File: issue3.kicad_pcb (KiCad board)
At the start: 2 copper layers, 213.1 x 129 mm, 206 parts, among them IC1 ULA, IC10 4116, IC11 4116, IC12 4116, IC13 4116, IC14 LM1889, IC15 4532, IC16 4532, IC17 4532, IC18 4532, IC19 4532, IC2 Z80, IC20 4532, IC21 4532, IC22 4532, IC23 LS32, IC24 LS00, IC25 LS157, IC26 LS157, IC3 LS157, IC4 LS157, IC5 ROM, IC6 4116, IC7 4116, IC8 4116, IC9 4116, J7 Barrel_Jack_MountingPin, T1 Transformer_1P_1S, X1 14Mhz, X2 4.43Mhz

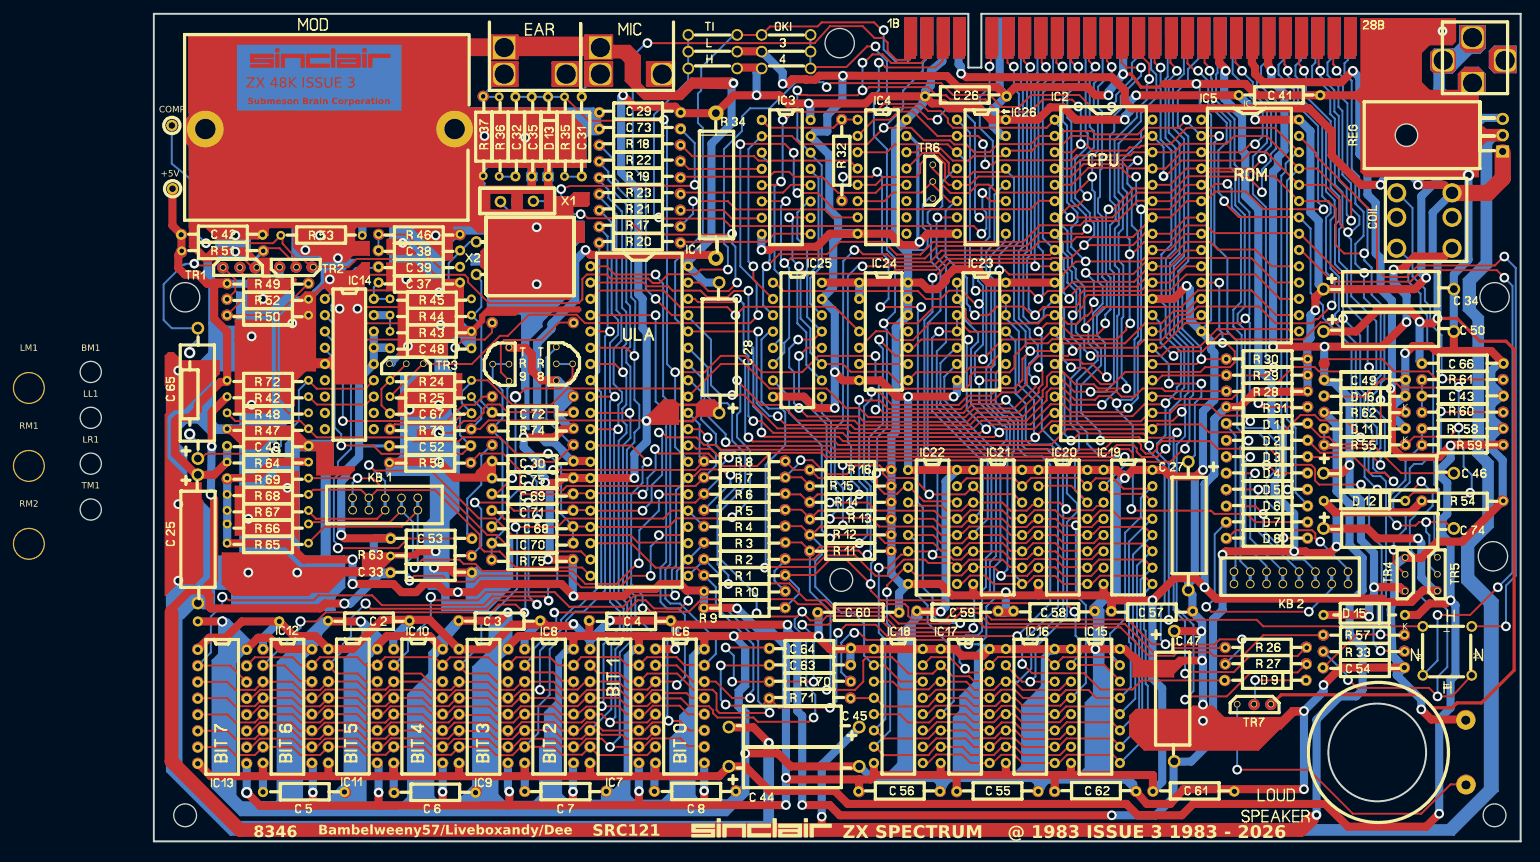
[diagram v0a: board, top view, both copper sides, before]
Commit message: Updated PCB size & Hole Positions
Updated PCB size & Hole Positions. Added stp's for components.
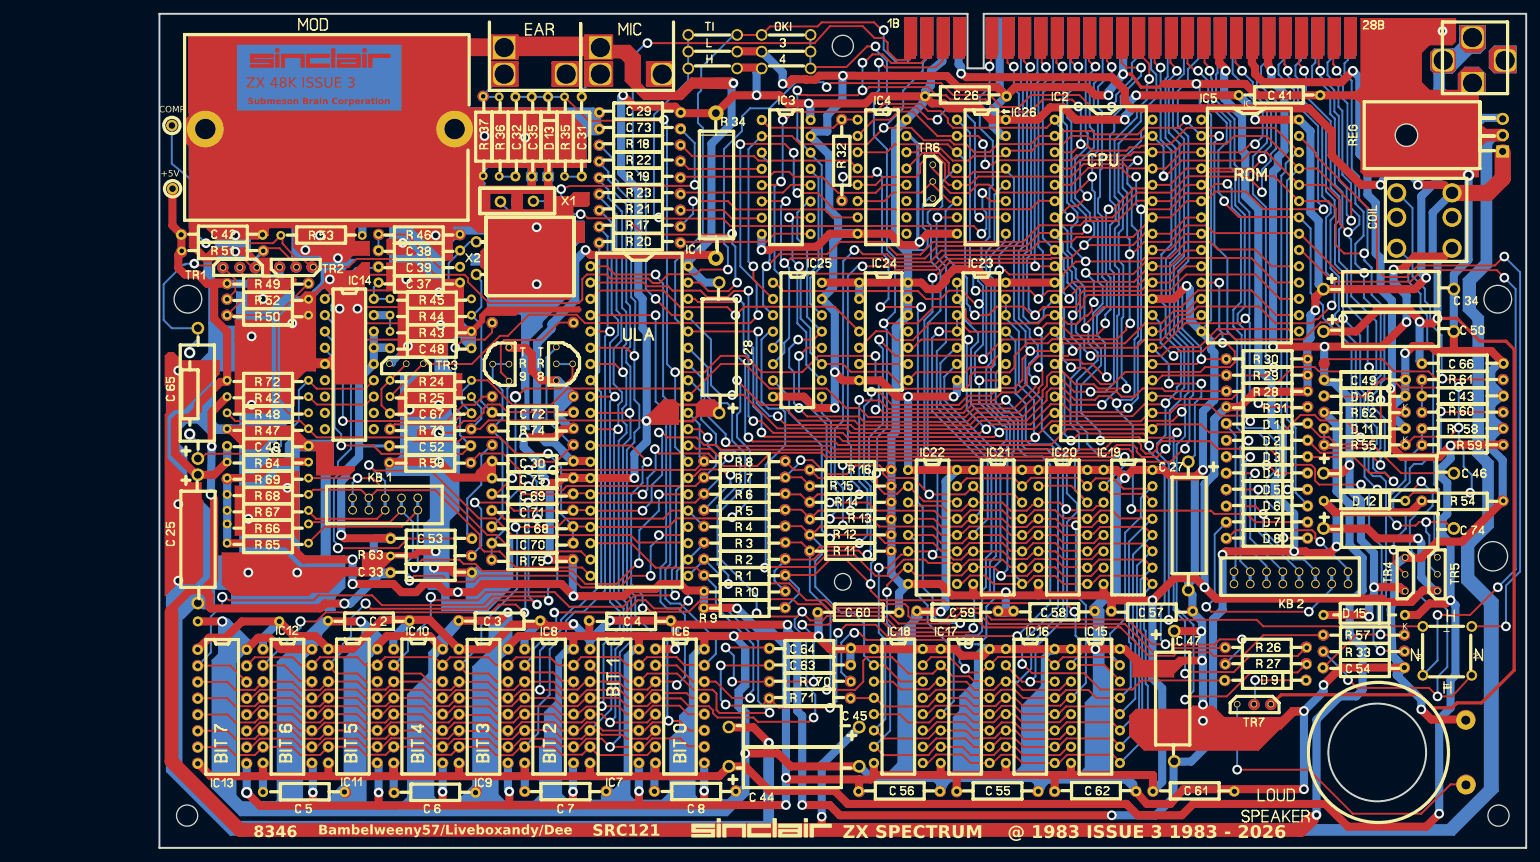
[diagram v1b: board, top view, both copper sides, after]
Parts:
- removed BM1, LL1, LR1, TM1: MountingHole, Mod:MountingHole_3.3mm Spectrum
- removed LM1, RM1, RM2: MountingHole, Mod:MountingHole_5mm Spectrum
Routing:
- net Net-(IC5-OE1L): track 111.9 -> 112.4 mm
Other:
- board size 213.1 x 129 mm -> 213.1 x 130 mm
